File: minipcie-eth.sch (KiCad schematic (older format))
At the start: 8 parts, among them J1 Conn_02x03_Odd_Even, J2 PMOD I2C 6pin, J3 Conn_02x03_Odd_Even, J4 PMOD UART 6pin, J5 PMOD UART 6pin, J6 Conn_02x03_Odd_Even, J7 Conn_02x03_Odd_Even, U1 VoCore_v2

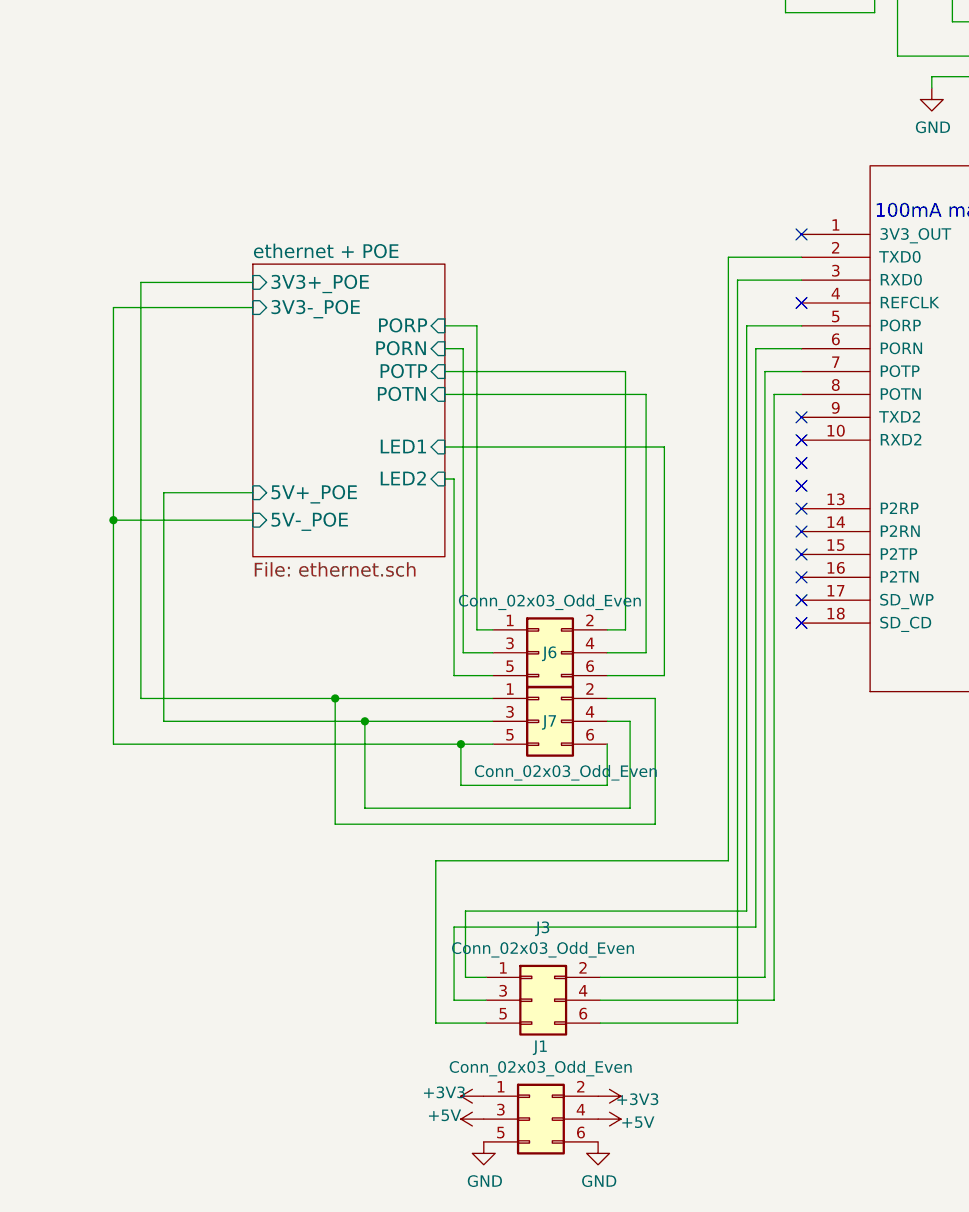
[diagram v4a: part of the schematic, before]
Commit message: Rearrangement to 90 degrees for the VoCore and routing complete. Fighting last 5 DRC violations and then on to double-checking dimensions and clearances
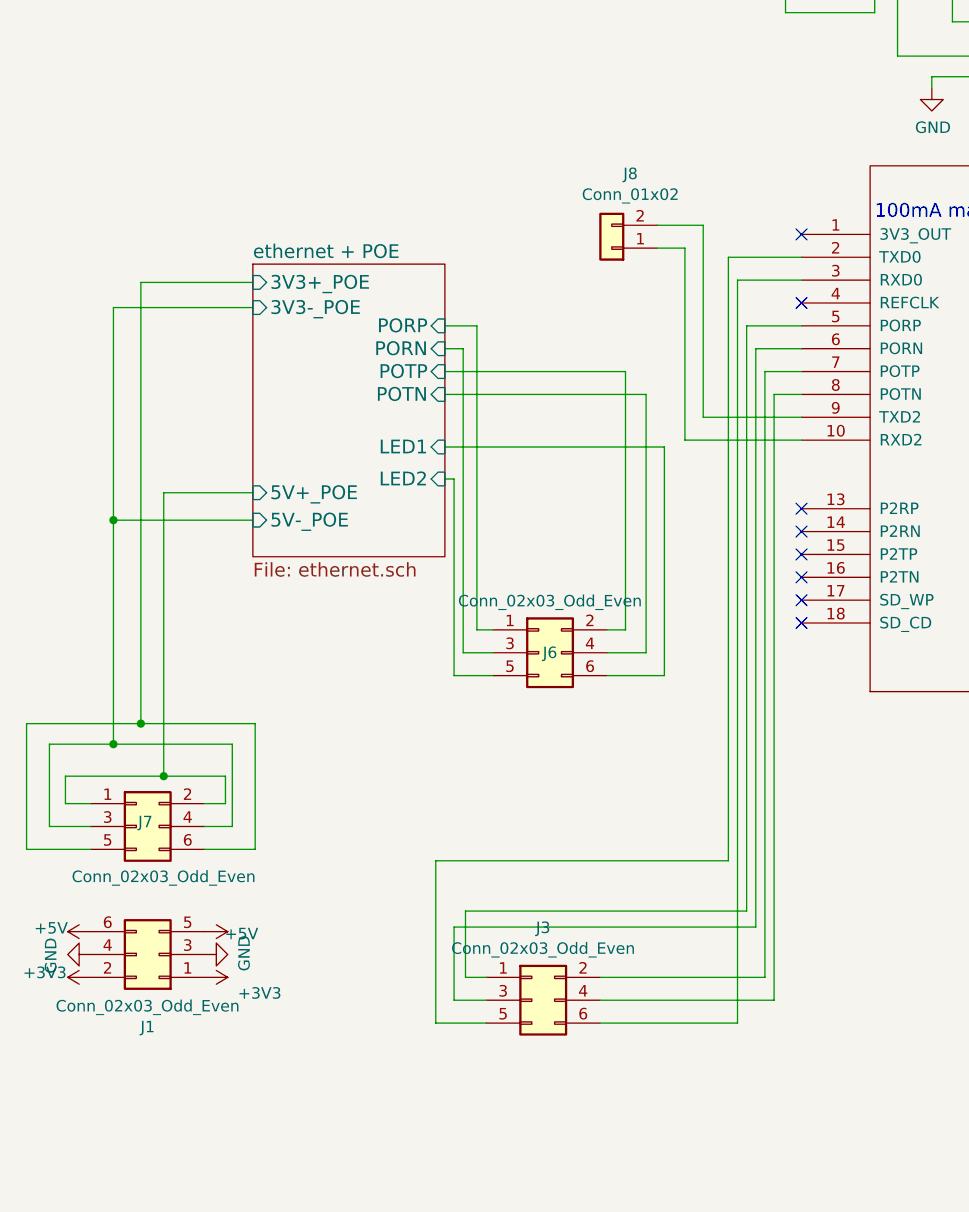
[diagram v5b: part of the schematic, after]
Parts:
- added J8: Conn_01x02, Connector_PinHeader_2.54mm:PinHeader_1x02_P2.54mm_Vertical, symbol Connector_Generic:Conn_01x02
- J6, J7: footprint Connector_PinHeader_2.54mm:PinHeader_2x03_P2.54mm_Vertical -> Connector_PinSocket_2.54mm:PinSocket_2x03_P2.54mm_Vertical
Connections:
- net +5V: now also J1.5 (Pin_5), J1.6 (Pin_6); no longer J1.3 (Pin_3), J1.4 (Pin_4)
- net GND: now also J1.3 (Pin_3), J1.4 (Pin_4); no longer J1.5 (Pin_5), J1.6 (Pin_6)
- net ethernet + POE/3V3+_POE: now also J7.5 (Pin_5), J7.6 (Pin_6); no longer J7.1 (Pin_1), J7.2 (Pin_2)
- net ethernet + POE/3V3-_POE: now also J7.3 (Pin_3), J7.4 (Pin_4); no longer J7.5 (Pin_5), J7.6 (Pin_6)
- net ethernet + POE/5V+_POE: now also J7.1 (Pin_1), J7.2 (Pin_2); no longer J7.3 (Pin_3), J7.4 (Pin_4)
- net at U1.10 (RXD2): now also J8.1 (Pin_1)
- net at U1.9 (TXD2): now also J8.2 (Pin_2)
- no-connect marks 26 -> 22
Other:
- moved on the sheet: J1, J7
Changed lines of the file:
@@
 	-1   0    0    1
 $EndComp
-NoConn ~ 4260 4180
-NoConn ~ 4260 4080
 NoConn ~ 4260 4280
 NoConn ~ 4260 4380
@@
 Wire Wire Line
 	5160 2390 5160 2480
-NoConn ~ 4260 3880
-NoConn ~ 4260 3980
 NoConn ~ 4260 4680
 NoConn ~ 4260 4780
@@
 L power1:GND #PWR0111
 U 1 1 5CD4BE9C
-P 2870 7050
-F 0 "#PWR0111" H 2870 6800 50  0001 C CNN
-F 1 "GND" H 2875 6877 50  0000 C CNN
-F 2 "" H 2870 7050 50  0001 C CNN
-F 3 "" H 2870 7050 50  0001 C CNN
-	1    2870 7050
-	1    0    0    -1
+P 1150 6230
+F 0 "#PWR0111" H 1150 5980 50  0001 C CNN
+F 1 "GND" H 1155 6057 50  0000 C CNN
+F 2 "" H 1150 6230 50  0001 C CNN
+F 3 "" H 1150 6230 50  0001 C CNN
+	1    1150 6230
+	0    1    1    0
 $EndComp
 $Comp
 L power1:GND #PWR0112
 U 1 1 5CD4C2C5
-P 3370 7050
-F 0 "#PWR0112" H 3370 6800 50  0001 C CNN
-F 1 "GND" H 3375 6877 50  0000 C CNN
-F 2 "" H 3370 7050 50  0001 C CNN
-F 3 "" H 3370 7050 50  0001 C CNN
-	1    3370 7050
-	1    0    0    -1
+P 1650 6230
+F 0 "#PWR0112" H 1650 5980 50  0001 C CNN
+F 1 "GND" H 1655 6057 50  0000 C CNN
+F 2 "" H 1650 6230 50  0001 C CNN
+F 3 "" H 1650 6230 50  0001 C CNN
+	1    1650 6230
+	0    -1   -1   0
 $EndComp
 Wire Wire Line
@@
 L power1:+3V3 #PWR0115
 U 1 1 5CE3B0C3
-P 2870 6850
-F 0 "#PWR0115" H 2870 6700 50  0001 C CNN
-F 1 "+3V3" V 2885 7023 50  0000 C CNN
-F 2 "" H 2870 6850 50  0001 C CNN
-F 3 "" H 2870 6850 50  0001 C CNN
-	1    2870 6850
+P 1150 6330
+F 0 "#PWR0115" H 1150 6180 50  0001 C CNN
+F 1 "+3V3" V 1170 6530 50  0000 C CNN
+F 2 "" H 1150 6330 50  0001 C CNN
+F 3 "" H 1150 6330 50  0001 C CNN
+	1    1150 6330
 	0    -1   -1   0
 $EndComp
@@
 L power1:+3V3 #PWR0116
 U 1 1 5CE3BC83
-P 3370 6850
-F 0 "#PWR0116" H 3370 6700 50  0001 C CNN
-F 1 "+3V3" V 3385 7023 50  0000 C CNN
-F 2 "" H 3370 6850 50  0001 C CNN
-F 3 "" H 3370 6850 50  0001 C CNN
-	1    3370 6850
+P 1650 6330
+F 0 "#PWR0116" H 1650 6180 50  0001 C CNN
+F 1 "+3V3" V 1720 6570 50  0000 C CNN
+F 2 "" H 1650 6330 50  0001 C CNN
+F 3 "" H 1650 6330 50  0001 C CNN
+	1    1650 6330
 	0    1    1    0
 $EndComp
@@
 	4140 3780 4140 6430
 Wire Wire Line
-	2910 5310 2770 5310
-Wire Wire Line
-	3410 5310 3410 5490
-Wire Wire Line
-	3410 5490 2770 5490
-Wire Wire Line
-	2770 5490 2770 5310
-Wire Wire Line
-	3410 5210 3510 5210
-Wire Wire Line
-	3510 5210 3510 5590
-Wire Wire Line
-	3510 5590 2350 5590
-Wire Wire Line
-	2910 5210 2350 5210
-Wire Wire Line
-	2910 5110 2220 5110
-Wire Wire Line
-	3410 5110 3620 5110
-Wire Wire Line
-	3620 5110 3620 5660
-Wire Wire Line
-	3620 5660 2220 5660
-Wire Wire Line
-	2220 5660 2220 5110
-Connection ~ 2220 5110
-Wire Wire Line
-	2350 5210 2350 5590
-Connection ~ 2350 5210
-Wire Wire Line
 	1860 3290 1370 3290
 Wire Wire Line
-	1370 3290 1370 5110
-Wire Wire Line
-	1370 5110 2220 5110
-Wire Wire Line
 	1860 4210 1470 4210
-Wire Wire Line
-	1470 4210 1470 5210
-Wire Wire Line
-	1470 5210 2350 5210
 NoConn ~ 4260 3080
 $Comp
 L power1:+5V #PWR0114
 U 1 1 5CD58DDB
-P 3370 6950
-F 0 "#PWR0114" H 3370 6800 50  0001 C CNN
-F 1 "+5V" V 3385 7123 50  0000 C CNN
-F 2 "" H 3370 6950 50  0001 C CNN
-F 3 "" H 3370 6950 50  0001 C CNN
-	1    3370 6950
+P 1650 6130
+F 0 "#PWR0114" H 1650 5980 50  0001 C CNN
+F 1 "+5V" V 1660 6290 50  0000 C CNN
+F 2 "" H 1650 6130 50  0001 C CNN
+F 3 "" H 1650 6130 50  0001 C CNN
+	1    1650 6130
 	0    1    1    0
 $EndComp
@@
 L power1:+5V #PWR0113
 U 1 1 5CD4C81C
-P 2870 6950
-F 0 "#PWR0113" H 2870 6800 50  0001 C CNN
-F 1 "+5V" V 2885 7123 50  0000 C CNN
-F 2 "" H 2870 6950 50  0001 C CNN
-F 3 "" H 2870 6950 50  0001 C CNN
-	1    2870 6950
+P 1150 6130
+F 0 "#PWR0113" H 1150 5980 50  0001 C CNN
+F 1 "+5V" V 1165 6303 50  0000 C CNN
+F 2 "" H 1150 6130 50  0001 C CNN
+F 3 "" H 1150 6130 50  0001 C CNN
+	1    1150 6130
 	0    -1   -1   0
 $EndComp
@@
 Wire Wire Line
 	8110 4300 8200 4300
-Connection ~ 2770 5310
-Wire Wire Line
-	1250 5310 2770 5310
 Wire Wire Line
 	1250 4330 1250 5310
@@
 L Connector_Generic:Conn_02x03_Odd_Even J1
 U 1 1 5D4C7761
-P 3070 6950
-F 0 "J1" H 3120 7267 50  0000 C CNN
-F 1 "Conn_02x03_Odd_Even" H 3120 7176 50  0000 C CNN
-F 2 "Connector_PinHeader_2.54mm:PinHeader_2x03_P2.54mm_Vertical" H 3070 6950 50  0001 C CNN
-F 3 "~" H 3070 6950 50  0001 C CNN
-	1    3070 6950
-	1    0    0    -1
+P 1450 6230
+F 0 "J1" H 1500 6547 50  0000 C CNN
+F 1 "Conn_02x03_Odd_Even" H 1500 6456 50  0000 C CNN
+F 2 "Connector_PinHeader_2.54mm:PinHeader_2x03_P2.54mm_Vertical" H 1450 6230 50  0001 C CNN
+F 3 "~" H 1450 6230 50  0001 C CNN
+	1    1450 6230
+	-1   0    0    1
 $EndComp
 $Comp
 L Connector_Generic:Conn_02x03_Odd_Even J7
 U 1 1 5D4DD4EF
-P 3110 5210
-F 0 "J7" H 3160 5210 50  0000 C CNN
-F 1 "Conn_02x03_Odd_Even" H 3230 4990 50  0000 C CNN
-F 2 "Connector_PinHeader_2.54mm:PinHeader_2x03_P2.54mm_Vertical" H 3110 5210 50  0001 C CNN
-F 3 "~" H 3110 5210 50  0001 C CNN
-	1    3110 5210
+P 1350 5670
+F 0 "J7" H 1390 5690 50  0000 C CNN
+F 1 "Conn_02x03_Odd_Even" H 1470 5450 50  0000 C CNN
+F 2 "Connector_PinSocket_2.54mm:PinSocket_2x03_P2.54mm_Vertical" H 1350 5670 50  0001 C CNN
+F 3 "~" H 1350 5670 50  0001 C CNN
+	1    1350 5670
 	1    0    0    -1
 $EndComp
@@
 F 0 "J6" H 3160 4910 50  0000 C CNN
 F 1 "Conn_02x03_Odd_Even" H 3160 5136 50  0000 C CNN
-F 2 "Connector_PinHeader_2.54mm:PinHeader_2x03_P2.54mm_Vertical" H 3110 4910 50  0001 C CNN
+F 2 "Connector_PinSocket_2.54mm:PinSocket_2x03_P2.54mm_Vertical" H 3110 4910 50  0001 C CNN
 F 3 "~" H 3110 4910 50  0001 C CNN
 	1    3110 4910
 	1    0    0    -1
 $EndComp
+$Comp
+L Connector_Generic:Conn_01x02 J8
+U 1 1 5D4DEB87
+P 3430 3140
+F 0 "J8" H 3348 2815 50  0000 C CNN
+F 1 "Conn_01x02" H 3348 2906 50  0000 C CNN
+F 2 "Connector_PinHeader_2.54mm:PinHeader_1x02_P2.54mm_Vertical" H 3430 3140 50  0001 C CNN
+F 3 "~" H 3430 3140 50  0001 C CNN
+	1    3430 3140
+	-1   0    0    1
+$EndComp
+Wire Wire Line
+	3630 3140 3750 3140
+Wire Wire Line
+	3750 3140 3750 3980
+Wire Wire Line
+	3750 3980 4260 3980
+Wire Wire Line
+	3630 3040 3830 3040
+Wire Wire Line
+	3830 3040 3830 3880
+Wire Wire Line
+	3830 3880 4260 3880
+Wire Wire Line
+	1470 5450 1040 5450
+Wire Wire Line
+	1040 5450 1040 5570
+Wire Wire Line
+	1040 5570 1150 5570
+Wire Wire Line
+	1470 4210 1470 5450
+Wire Wire Line
+	1470 5450 1740 5450
+Wire Wire Line
+	1740 5450 1740 5570
+Wire Wire Line
+	1740 5570 1650 5570
+Connection ~ 1470 5450
+Wire Wire Line
+	1250 5310 970  5310
+Wire Wire Line
+	1250 5310 1770 5310
+Wire Wire Line
+	1770 5310 1770 5670
+Wire Wire Line
+	1770 5670 1650 5670
+Connection ~ 1250 5310
+Wire Wire Line
+	970  5310 970  5670
+Wire Wire Line
+	970  5670 1150 5670
+Wire Wire Line
+	1370 5220 870  5220
+Wire Wire Line
+	870  5220 870  5770
+Wire Wire Line
+	870  5770 1150 5770
+Wire Wire Line
+	1370 3290 1370 5220
+Wire Wire Line
+	1650 5770 1870 5770
+Wire Wire Line
+	1870 5770 1870 5220
+Wire Wire Line
+	1870 5220 1370 5220
+Connection ~ 1370 5220
 $EndSCHEMATC

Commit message: Add README and some nice pictures
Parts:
- J5: value PMOD UART 6pin -> PMOD GPIO 6pin
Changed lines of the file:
@@
 P 8400 4200
 F 0 "J5" H 8480 4192 50  0000 L CNN
-F 1 "PMOD UART 6pin" H 8480 4101 50  0000 L CNN
+F 1 "PMOD GPIO 6pin" H 8480 4101 50  0000 L CNN
 F 2 "Connector_PinHeader_2.54mm:PinHeader_1x06_P2.54mm_Horizontal" H 8400 4200 50  0001 C CNN
 F 3 "~" H 8400 4200 50  0001 C CNN
